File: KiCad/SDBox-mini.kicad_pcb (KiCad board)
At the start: 2 copper layers, 36.7 x 34 mm, 31 parts, among them J1 DB25_Male, J2 Conn_01x06, J3 Micro_SD_Card, J4 USB_B_Micro, Q1 BC857CW, U1 ATmega328P-AU, U2 LM1117-3.3, U3 74LVC3G17, U4 74HCT2G17, Y1 Crystal_GND24_Small

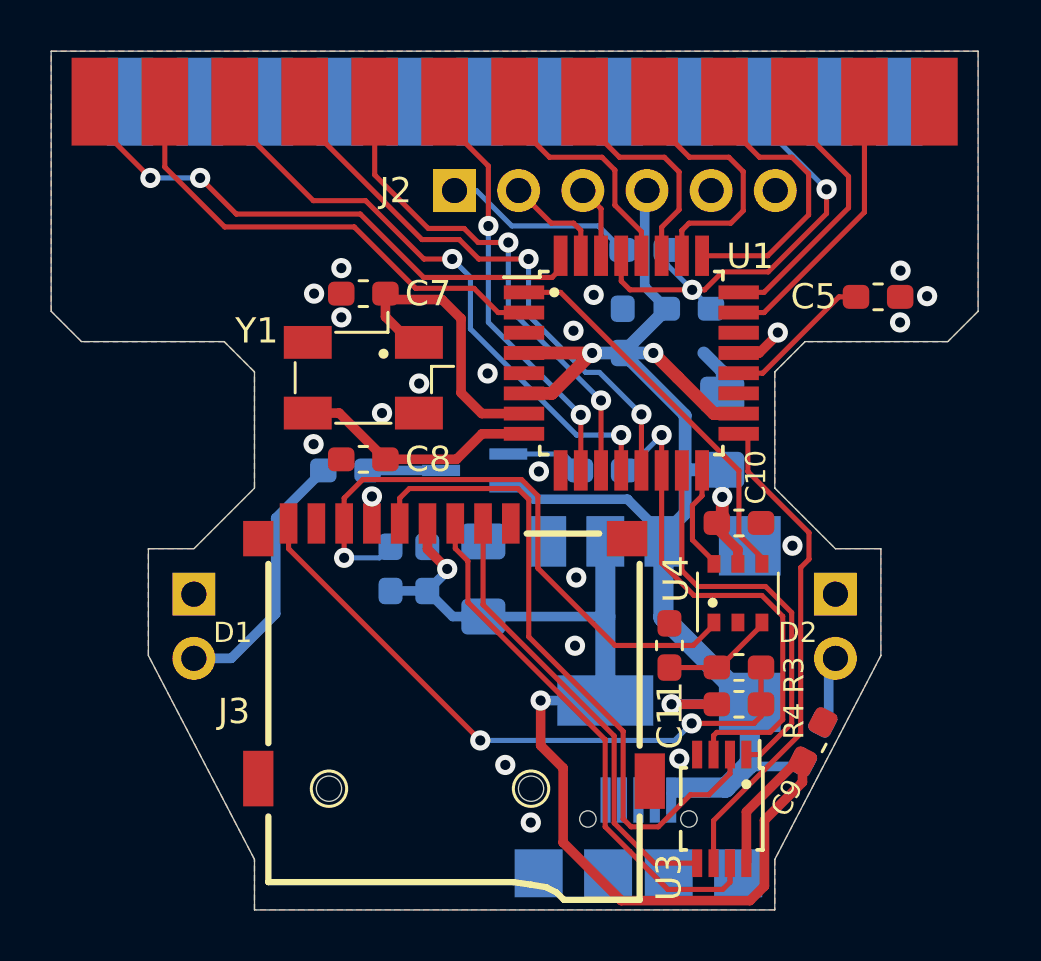
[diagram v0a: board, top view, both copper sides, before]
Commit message: added silkscreen texts and oshw-symbol
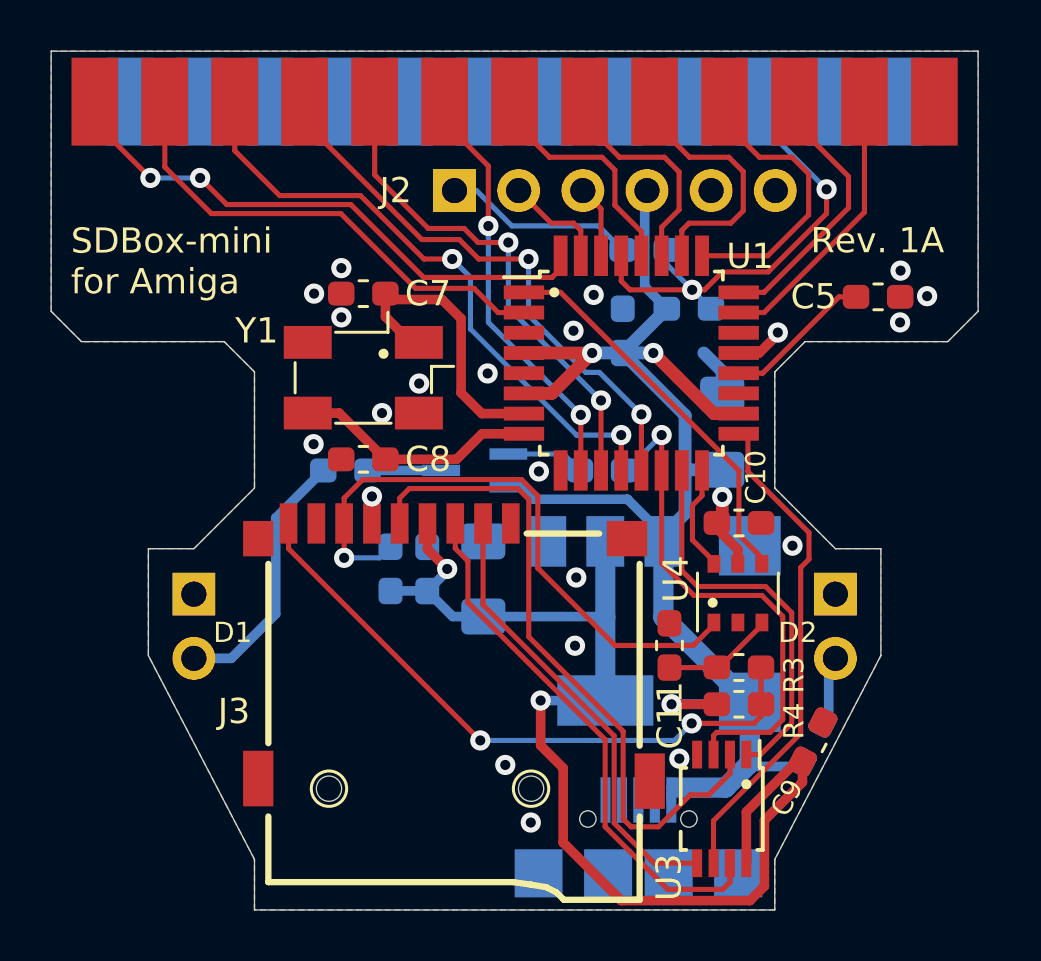
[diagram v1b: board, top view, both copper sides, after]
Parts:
- added REF**: OSHW-Symbol_6.7x6mm_SilkScreen, Symbol:OSHW-Symbol_6.7x6mm_SilkScreen, B.Cu at (99.2, 78.9)
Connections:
- J1 pad 1: (no net) -> Net-(J1-Pad1)
- J1 pad 14: (no net) -> Net-(J1-Pad14)
- J1 pad 15: (no net) -> Net-(J1-Pad15)
- J1 pad 23: (no net) -> Net-(J1-Pad23)
- J1 pad 24: (no net) -> Net-(J1-Pad24)
- J1 pad 25: (no net) -> Net-(J1-Pad25)
- J3 pad 1: (no net) -> Net-(J3-Pad1)
- J3 pad 8: (no net) -> Net-(J3-Pad8)
- J4 pad 2: (no net) -> Net-(J4-Pad2)
- J4 pad 3: (no net) -> Net-(J4-Pad3)
- J4 pad 4: (no net) -> Net-(J4-Pad4)
- U1 pad 19: (no net) -> Net-(U1-Pad19)
- U1 pad 22: (no net) -> Net-(U1-Pad22)
- U1 pad 9: (no net) -> Net-(U1-Pad9)
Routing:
- net BUSY: track 23.8 -> 24.5 mm
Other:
- board text added: "Design by J.Bilander FW by N.Ekström (C) 2021"
- board text added: "Rev. 1A"
- board text added: "SDBox-mini for Amiga"

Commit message: Changed pin assignment BUSY from PB0 to PD4, POUT from PD4 to PD5 and rerouted due to change in FW.
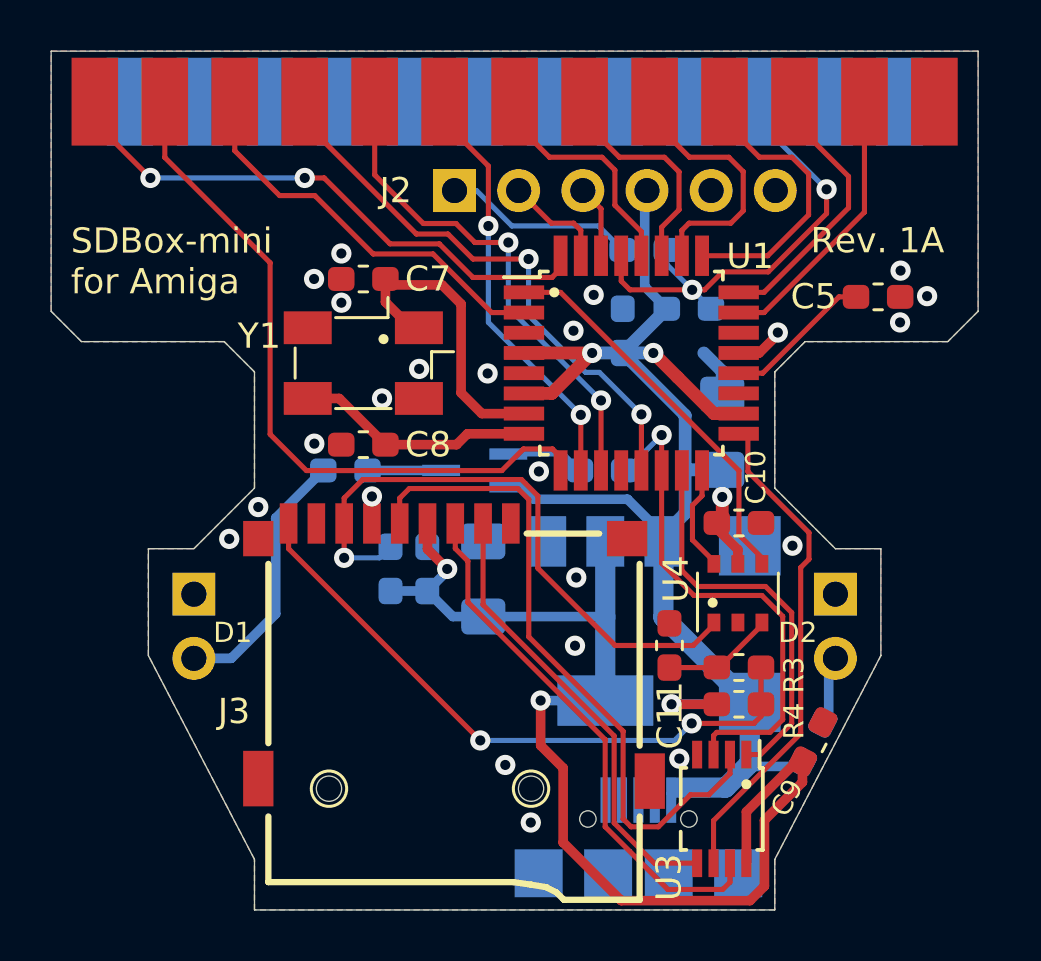
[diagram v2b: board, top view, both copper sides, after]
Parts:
- moved C7 0.58 mm to (100.5, 59.0)
- moved C8 0.58 mm to (100.5, 65.6)
- moved Y1 0.58 mm to (100.5, 62.4)
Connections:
- U1 pad 12: BUSY -> Net-(U1-Pad12)
- U1 pad 2: POUT -> BUSY
- U1 pad 9: Net-(U1-Pad9) -> POUT
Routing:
- net POUT: track 19.2 -> 28.0 mm
- net BUSY: track 24.5 -> 16.0 mm, vias 2 -> 0
- net /XTAL1: track 11.8 -> 12.4 mm
- net GND: vias 21 -> 23

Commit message: removed FTDI-header, added ICSP-header, removed hw-debounce circuit and rerouted
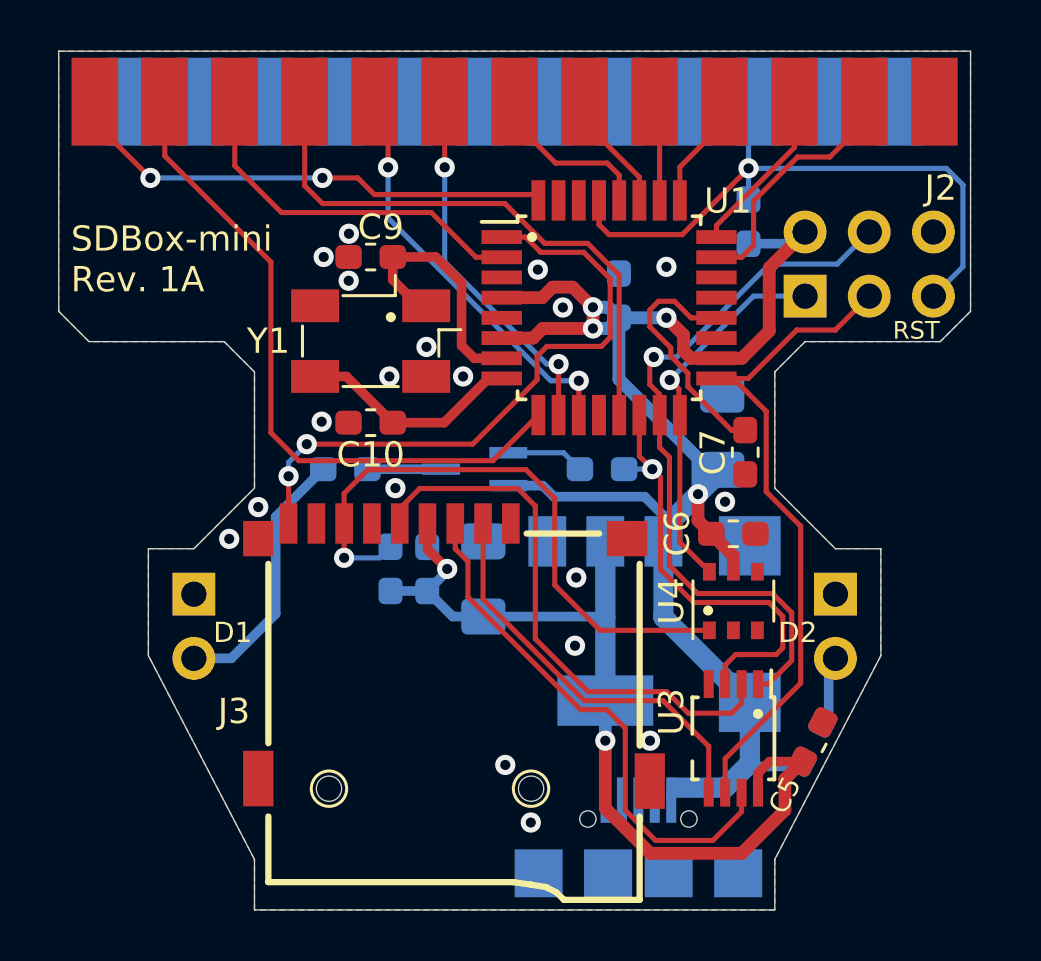
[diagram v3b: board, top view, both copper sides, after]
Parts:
- removed C11: 0.1uF, Capacitor_SMD:C_0603_1608Metric_Pad1.05x0.95mm_HandSolder
- removed the C4 at (111.7, 57.9)
- removed the C5 at (120.9, 59.7)
- removed the C8 at (100.5, 65.6)
- removed the R3 at (115.4, 74.4)
- removed the R4 at (115.4, 75.9)
- added C6: 0.1uF, Capacitor_SMD:C_0603_1608Metric_Pad1.05x0.95mm_HandSolder, F.Cu at (115.2, 69.1)
- added C9: 16pF, Capacitor_SMD:C_0603_1608Metric_Pad1.05x0.95mm_HandSolder, F.Cu at (100.8, 58.1)
- C10: value 0.1uF -> 16pF
- C7: value 16pF -> 0.1uF
- J2: value Conn_01x06 -> Conn_02x03_Odd_Even; footprint Connector_PinHeader_2.54mm:PinHeader_1x06_P2.54mm_Vertical -> Connector_PinHeader_2.54mm:PinHeader_2x03_P2.54mm_Vertical
- moved C7 16.6 mm to (115.6, 65.9), turned to 90 degrees
- moved C10 15.1 mm to (100.8, 64.7), turned to 180 degrees
- moved J2 14.5 mm to (118.0, 59.7)
- moved R1 4.18 mm to (115.8, 56.8), turned to 270 degrees
- moved U3 2.83 mm to (115.2, 77.2)
- moved U1 2.36 mm to (110.2, 60.2)
- moved C8 1.40 mm to (110.6, 59.7)
- moved Y1 0.92 mm to (100.8, 61.5)
- moved U4 0.36 mm to (115.2, 71.8)
- renumbered C12 to C4, C9 to C5, C6 to C8, R5 to R3, R6 to R4, R7 to R5
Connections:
- C10 pad 1: VCC -> /XTAL2
- C7 pad 1: /XTAL1 -> GND
- C7 pad 2: GND -> /AREF
- J2 pad 1: DTR -> MISO
- J2 pad 2: TXO -> VCC
- J2 pad 3: RXI -> SCK
- J2 pad 4: VCC -> MOSI
- J2 pad 5: GND -> RESET
- J3 pad 9: CD -> CP
- U1 pad 30: RXI -> Net-(U1-Pad30)
- U1 pad 31: TXO -> Net-(U1-Pad31)
- U4 pad 3: Net-(C11-Pad1) -> GND
- U4 pad 4: CP -> Net-(U4-Pad4)
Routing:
- net CD: track 25.2 -> 0.00 mm, vias 2 -> 0
- net MOSI: track 15.7 -> 28.5 mm, vias 0 -> 1
- net MISO: track 4.21 -> 15.0 mm, vias 0 -> 1
- net 3V3: track 46.9 -> 36.3 mm
- net CP: track 15.5 -> 25.0 mm, vias 0 -> 2
- net DTR: track 7.63 -> 0.00 mm
- net SCK: track 19.9 -> 26.8 mm
- net D2: track 11.5 -> 4.64 mm
- net RESET: track 19.1 -> 25.8 mm, vias 2 -> 1
- net D3: track 10.4 -> 3.99 mm
- net SCK_3V3: track 26.6 -> 22.1 mm
- net Net-(C11-Pad1): track 4.46 -> 0.00 mm
- net D1: track 10.8 -> 6.64 mm
- net D4: track 8.98 -> 4.81 mm
- net SELECT: track 23.0 -> 18.8 mm
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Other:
- board size 36.7 x 34 mm -> 36.1 x 34 mm
- board text added: "RST"
- board text added: "SDBox-mini Rev. 1A"
- board text removed: "Rev. 1A"
- board text removed: "SDBox-mini for Amiga"

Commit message: Improved 3V3 and other small cosmetic fixes
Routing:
- net POUT: track 26.6 -> 27.4 mm
- net GND: vias 19 -> 17
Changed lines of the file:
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@@
     (thickness 1.6)
     (drawings 25)
-    (tracks 318)
+    (tracks 315)
     (zones 0)
     (modules 28)
@@
   )
   (setup
-    (last_trace_width 0.2032)
+    (last_trace_width 0.508)
     (user_trace_width 0.1524)
     (user_trace_width 0.1778)
@@
   (via (at 101.54 62.88) (size 0.8) (drill 0.4) (layers F.Cu B.Cu) (net 1))
   (via (at 101.78 67.3) (size 0.8) (drill 0.4) (layers F.Cu B.Cu) (net 1))
-  (via (at 107.14 80.54) (size 0.8) (drill 0.4) (layers F.Cu B.Cu) (net 1))
-  (via (at 106.13 78.26) (size 0.8) (drill 0.4) (layers F.Cu B.Cu) (net 1))
   (via (at 96.35 68.05) (size 0.8) (drill 0.4) (layers F.Cu B.Cu) (net 1))
   (via (at 95.2 69.31) (size 0.8) (drill 0.4) (layers F.Cu B.Cu) (net 1))
@@
   (segment (start 107.20878 55.67878) (end 107.44 55.91) (width 0.2032) (layer F.Cu) (net 4))
   (segment (start 100.29 55.02) (end 100.94878 55.67878) (width 0.2032) (layer F.Cu) (net 4))
-  (segment (start 105.635999 66.214001) (end 107.44 64.41) (width 0.2032) (layer F.Cu) (net 5))
-  (segment (start 97.956079 66.214001) (end 105.635999 66.214001) (width 0.2032) (layer F.Cu) (net 5))
+  (segment (start 107.44 65.68) (end 107.44 64.41) (width 0.2032) (layer F.Cu) (net 5))
+  (segment (start 106.905999 66.214001) (end 107.44 65.68) (width 0.2032) (layer F.Cu) (net 5))
+  (segment (start 97.956079 66.214001) (end 106.905999 66.214001) (width 0.2032) (layer F.Cu) (net 5))
+  (segment (start 92.65 52) (end 92.65 54.15) (width 0.2032) (layer F.Cu) (net 5))
   (segment (start 96.85 65.107922) (end 97.956079 66.214001) (width 0.2032) (layer F.Cu) (net 5))
+  (segment (start 96.85 58.35) (end 96.85 65.107922) (width 0.2032) (layer F.Cu) (net 5))
   (segment (start 92.65 54.15) (end 96.85 58.35) (width 0.2032) (layer F.Cu) (net 5))
-  (segment (start 96.85 58.35) (end 96.85 65.107922) (width 0.2032) (layer F.Cu) (net 5))
-  (segment (start 92.65 52) (end 92.65 54.15) (width 0.2032) (layer F.Cu) (net 5))
   (segment (start 104.97 58.16) (end 105.99 58.16) (width 0.2032) (layer F.Cu) (net 6))
   (segment (start 95.42 52) (end 95.42 54.54) (width 0.2032) (layer F.Cu) (net 6))
@@
   (segment (start 112.01 62.11) (end 112.92 62.11) (width 0.2032) (layer B.Cu) (net 20))
   (via (at 103.83 70.5) (size 0.8) (drill 0.4) (layers F.Cu B.Cu) (net 21))
-  (segment (start 103.05 69.72) (end 103.05 68.7) (width 0.381) (layer F.Cu) (net 21))
-  (segment (start 103.83 70.5) (end 103.05 69.72) (width 0.381) (layer F.Cu) (net 21))
-  (segment (start 104.05 72.385) (end 103.04 71.375) (width 0.381) (layer B.Cu) (net 21))
-  (segment (start 105.26 72.385) (end 104.05 72.385) (width 0.381) (layer B.Cu) (net 21))
-  (segment (start 103.83 70.585) (end 103.04 71.375) (width 0.381) (layer B.Cu) (net 21))
-  (segment (start 103.83 70.5) (end 103.83 70.585) (width 0.381) (layer B.Cu) (net 21))
   (segment (start 110.075 72.385) (end 110.09 72.4) (width 0.381) (layer B.Cu) (net 21))
-  (segment (start 105.26 72.385) (end 110.075 72.385) (width 0.381) (layer B.Cu) (net 21))
   (segment (start 110.09 72.4) (end 110.09 75.71) (width 0.8) (layer B.Cu) (net 21))
   (segment (start 110.09 69.41) (end 110.09 72.4) (width 0.8) (layer B.Cu) (net 21))
-  (segment (start 103.0378 71.3728) (end 103.04 71.375) (width 0.381) (layer B.Cu) (net 21))
-  (segment (start 101.5866 71.3728) (end 103.0378 71.3728) (width 0.381) (layer B.Cu) (net 21))
   (via (at 110.09 77.3) (size 0.8) (drill 0.4) (layers F.Cu B.Cu) (net 21))
   (segment (start 117.89597 78.126134) (end 116.593866 78.126134) (width 0.381) (layer F.Cu) (net 21))
@@
   (segment (start 110.09 79.978434) (end 111.869576 81.75801) (width 0.508) (layer F.Cu) (net 21))
   (segment (start 110.09 77.3) (end 110.09 79.978434) (width 0.508) (layer F.Cu) (net 21))
+  (segment (start 105.26 72.385) (end 110.075 72.385) (width 0.8) (layer B.Cu) (net 21))
+  (segment (start 104.05 72.385) (end 103.04 71.375) (width 0.508) (layer B.Cu) (net 21))
+  (segment (start 105.26 72.385) (end 104.05 72.385) (width 0.508) (layer B.Cu) (net 21))
+  (segment (start 102.9572 71.3728) (end 103.83 70.5) (width 0.508) (layer B.Cu) (net 21))
+  (segment (start 101.5866 71.3728) (end 102.9572 71.3728) (width 0.508) (layer B.Cu) (net 21))
+  (segment (start 103.05 69.72) (end 103.05 68.7) (width 0.508) (layer F.Cu) (net 21))
+  (segment (start 103.83 70.5) (end 103.05 69.72) (width 0.508) (layer F.Cu) (net 21))
   (segment (start 115.485 80.1132) (end 115.485 79.36) (width 0.2032) (layer F.Cu) (net 22))
   (segment (start 114.348201 81.249999) (end 115.485 80.1132) (width 0.2032) (layer F.Cu) (net 22))

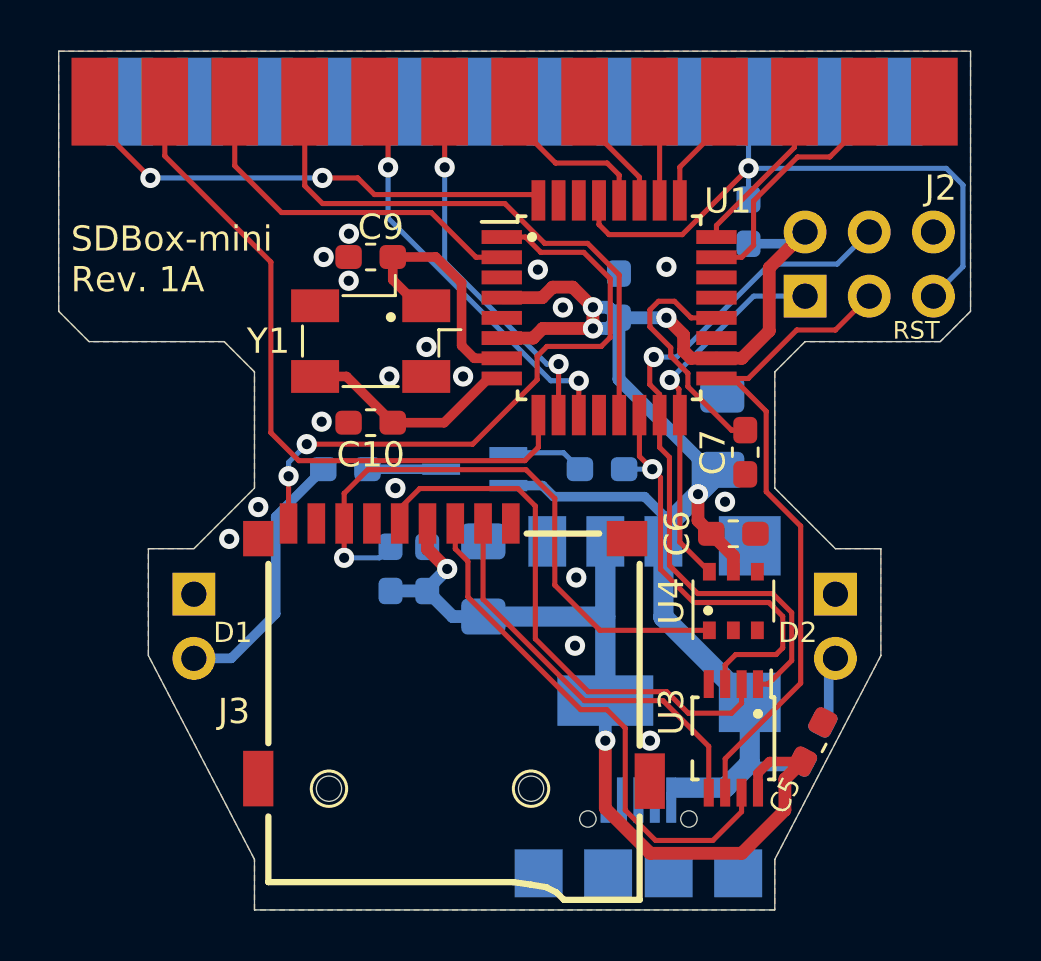
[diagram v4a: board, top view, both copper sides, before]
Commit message: removed transistor Q1, changed Activity LED circuit to sink by SS
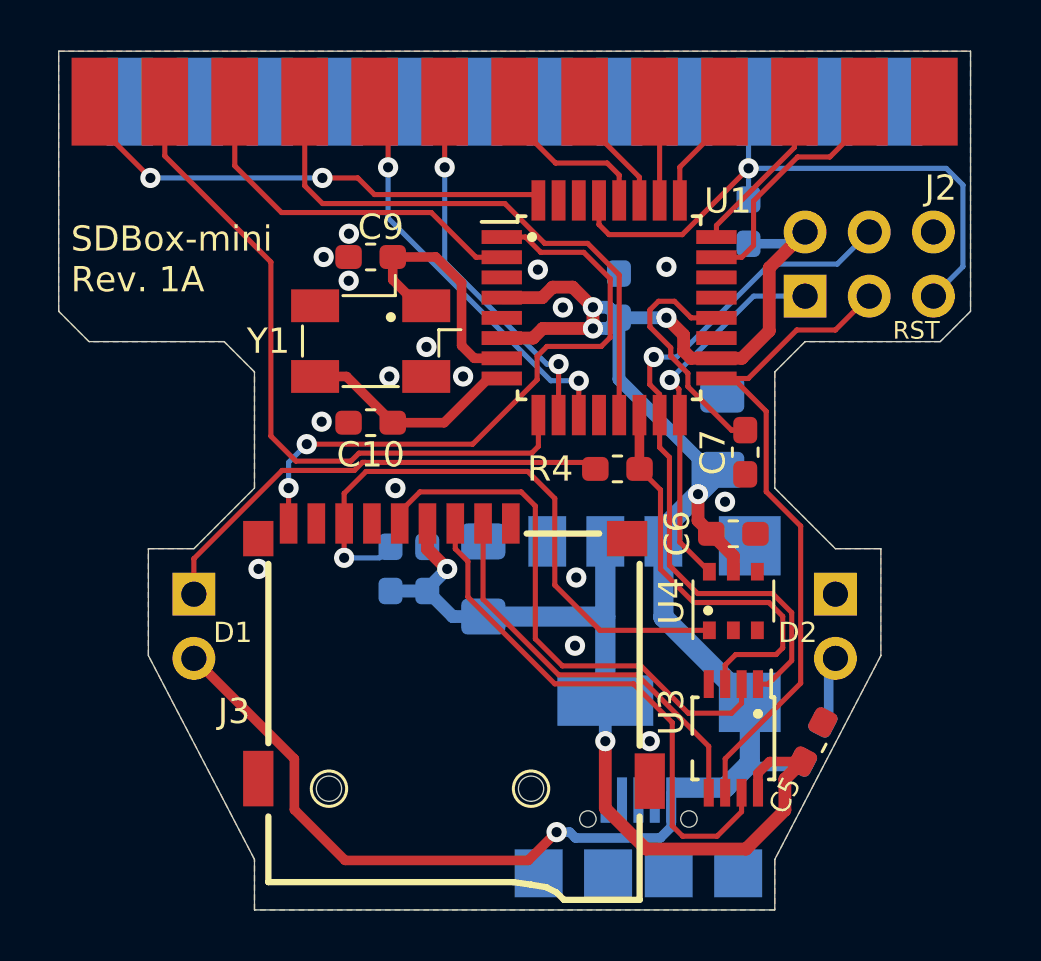
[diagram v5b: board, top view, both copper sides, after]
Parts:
- removed Q1: BC857CW, Package_TO_SOT_SMD:SOT-323_SC-70_Handsoldering
- removed R5: 10k, Resistor_SMD:R_0603_1608Metric_Pad1.05x0.95mm_HandSolder
- R4: moved to F.Cu
- moved R4 10.8 mm to (110.6, 66.5), turned to 180 degrees
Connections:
- D1 pad 1: GND -> Net-(D1-Pad1)
- D1 pad 2: Net-(D1-Pad2) -> VCC
- R4 pad 1: Net-(D1-Pad2) -> SS
- R4 pad 2: Net-(Q1-Pad3) -> Net-(D1-Pad1)
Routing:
- net Net-(D1-Pad1): track 0.00 -> 19.0 mm
- net VCC: track 68.1 -> 85.7 mm, vias 4 -> 5
- net Net-(D1-Pad2): track 10.5 -> 0.00 mm
- net Net-(Q1-Pad1): track 3.10 -> 0.00 mm
- net Net-(Q1-Pad3): track 2.92 -> 0.00 mm
- net SS: track 17.7 -> 16.6 mm, vias 1 -> 0
- net GND: vias 17 -> 16
